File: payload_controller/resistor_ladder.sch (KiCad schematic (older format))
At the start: 35 parts, among them U1 74HC590, U10 ADG841YKSZ-500RL7, U10 OPA2387, U11 ADG841YKSZ-500RL7, U11 MCP4725xxx-xCH, U12 ADG841YKSZ-500RL7, U13 ADG841YKSZ-500RL7, U6 ADG841YKSZ-500RL7, U7 ADG841YKSZ-500RL7, U8 ADG841YKSZ-500RL7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

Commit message: Continuing layout
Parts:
- removed U10: OPA2387, Package_SON:WSON-8-1EP_2x2mm_P0.5mm_EP0.9x1.6mm, symbol OPA2387:OPA2387
- added unit 2 of U10
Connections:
- net -3V3: now also U10.9 (TP)
- net V_PANEL: now also U10.5 (+), U10.7
- net at R11.2, R13.1, R14.1: now also U10.6 (-)
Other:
- moved on the sheet: R13, R14
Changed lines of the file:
@@
 	-1   0    0    1
-$EndComp
-$Comp
-L Device:R R14
-U 1 1 6395E4CC
-P 9550 2700
-F 0 "R14" V 9650 2700 50  0000 C CNN
-F 1 "100k" V 9550 2700 50  0000 C CNN
-F 2 "Resistor_SMD:R_0603_1608Metric" V 9480 2700 50  0001 C CNN
-F 3 "~" H 9550 2700 50  0001 C CNN
-	1    9550 2700
-	0    -1   -1   0
-$EndComp
-$Comp
-L power:GND #PWR0134
-U 1 1 6395EDA9
-P 9700 2700
-F 0 "#PWR0134" H 9700 2450 50  0001 C CNN
-F 1 "GND" H 9705 2527 50  0000 C CNN
-F 2 "" H 9700 2700 50  0001 C CNN
-F 3 "" H 9700 2700 50  0001 C CNN
-	1    9700 2700
-	0    -1   -1   0
 $EndComp
 Wire Wire Line
@@
 Wire Wire Line
 	9500 1350 9500 1550
-$Comp
-L power:-3V3 #PWR?
-U 1 1 638EAACA
-P 9700 2500
-AR Path="/63C503EE/638EAACA" Ref="#PWR?"  Part="1"
-AR Path="/635FEB2F/638EAACA" Ref="#PWR0136"  Part="1"
-F 0 "#PWR0136" H 9700 2600 50  0001 C CNN
-F 1 "-3V3" V 9715 2628 50  0000 L CNN
-F 2 "" H 9700 2500 50  0001 C CNN
-F 3 "" H 9700 2500 50  0001 C CNN
-	1    9700 2500
-	0    1    1    0
-$EndComp
 Wire Wire Line
 	9650 2300 10000 2300
@@
 Wire Wire Line
 	10000 1550 9500 1550
-$Comp
-L Device:R R13
-U 1 1 6391F434
-P 9550 2500
-F 0 "R13" V 9650 2500 50  0000 C CNN
-F 1 "500k" V 9550 2500 50  0000 C CNN
-F 2 "Resistor_SMD:R_0603_1608Metric" V 9480 2500 50  0001 C CNN
-F 3 "~" H 9550 2500 50  0001 C CNN
-	1    9550 2500
-	0    -1   -1   0
-$EndComp
 Connection ~ 9500 1350
 Wire Wire Line
 	9500 1350 9950 1350
-Wire Wire Line
-	9350 2300 9350 2500
-Wire Wire Line
-	9400 2700 9350 2700
-Wire Wire Line
-	9400 2500 9350 2500
-Connection ~ 9350 2500
-Wire Wire Line
-	9350 2500 9350 2700
-Wire Wire Line
-	9350 2800 9350 2700
-Connection ~ 9350 2700
 Wire Wire Line
 	9450 3900 9450 4100
@@
 	9350 3900 9350 5650
 Wire Notes Line
-	8750 1450 8750 4850
+	8650 1450 8650 4850
 Wire Notes Line
 	8750 4850 10350 4850
@@
 	1700 3750 2050 3750
 $Comp
-L OPA2387:OPA2387 U10
-U 1 1 6382E466
-P 9500 2050
-F 0 "U10" V 9800 1950 50  0000 R CNN
-F 1 "OPA2387" V 9700 1950 50  0000 R CNN
-F 2 "Package_SON:WSON-8-1EP_2x2mm_P0.5mm_EP0.9x1.6mm" H 9900 2250 50  0001 C CNN
-F 3 "" H 9900 2250 50  0001 C CNN
-	1    9500 2050
-	0    -1   -1   0
-$EndComp
-Connection ~ 9500 1550
-$Comp
 L power:-3V3 #PWR?
 U 1 1 6383D96E
-P 9850 1950
+P 9500 2300
 AR Path="/63C503EE/6383D96E" Ref="#PWR?"  Part="1"
 AR Path="/635FEB2F/6383D96E" Ref="#PWR0128"  Part="1"
-F 0 "#PWR0128" H 9850 2050 50  0001 C CNN
-F 1 "-3V3" V 9865 2078 50  0000 L CNN
-F 2 "" H 9850 1950 50  0001 C CNN
-F 3 "" H 9850 1950 50  0001 C CNN
-	1    9850 1950
+F 0 "#PWR0128" H 9500 2400 50  0001 C CNN
+F 1 "-3V3" V 9515 2428 50  0000 L CNN
+F 2 "" H 9500 2300 50  0001 C CNN
+F 3 "" H 9500 2300 50  0001 C CNN
+	1    9500 2300
 	-1   0    0    1
 $EndComp
-$Comp
-L power:+3V3 #PWR0135
-U 1 1 6383DF99
-P 9150 1950
-F 0 "#PWR0135" H 9150 1800 50  0001 C CNN
-F 1 "+3V3" H 9165 2123 50  0000 C CNN
-F 2 "" H 9150 1950 50  0001 C CNN
-F 3 "" H 9150 1950 50  0001 C CNN
-	1    9150 1950
-	1    0    0    -1
-$EndComp
-Wire Wire Line
-	9850 1950 9800 1950
-Wire Wire Line
-	9150 1950 9200 1950
 Connection ~ 3950 1750
 Wire Wire Line
@@
 	0    1    1    0
 $EndComp
+$Comp
+L OPA2387:OPA2387 U?
+U 2 1 63A95D48
+P 9500 2050
+AR Path="/63C503EE/63A95D48" Ref="U?"  Part="2"
+AR Path="/635FEB2F/63A95D48" Ref="U10"  Part="2"
+F 0 "U10" H 9750 2350 50  0000 C CNN
+F 1 "OPA2387" H 9800 2250 50  0000 C CNN
+F 2 "Package_SON:WSON-8-1EP_2x2mm_P0.5mm_EP0.9x1.6mm" H 9900 2250 50  0001 C CNN
+F 3 "" H 9900 2250 50  0001 C CNN
+	2    9500 2050
+	0    1    -1   0
+$EndComp
+Connection ~ 9500 1550
+Connection ~ 9350 2700
+Connection ~ 9350 2500
+Wire Wire Line
+	9350 2300 9350 2500
+Wire Wire Line
+	9350 2800 9350 2700
+Wire Wire Line
+	9350 2500 9350 2700
+Wire Wire Line
+	9300 2700 9350 2700
+Wire Wire Line
+	9300 2500 9350 2500
+$Comp
+L Device:R R13
+U 1 1 6391F434
+P 9150 2700
+F 0 "R13" V 9250 2700 50  0000 C CNN
+F 1 "500k" V 9150 2700 50  0000 C CNN
+F 2 "Resistor_SMD:R_0603_1608Metric" V 9080 2700 50  0001 C CNN
+F 3 "~" H 9150 2700 50  0001 C CNN
+	1    9150 2700
+	0    1    1    0
+$EndComp
+$Comp
+L power:-3V3 #PWR?
+U 1 1 638EAACA
+P 9000 2700
+AR Path="/63C503EE/638EAACA" Ref="#PWR?"  Part="1"
+AR Path="/635FEB2F/638EAACA" Ref="#PWR0136"  Part="1"
+F 0 "#PWR0136" H 9000 2800 50  0001 C CNN
+F 1 "-3V3" V 9015 2828 50  0000 L CNN
+F 2 "" H 9000 2700 50  0001 C CNN
+F 3 "" H 9000 2700 50  0001 C CNN
+	1    9000 2700
+	0    -1   -1   0
+$EndComp
+$Comp
+L power:GND #PWR0134
+U 1 1 6395EDA9
+P 9000 2500
+F 0 "#PWR0134" H 9000 2250 50  0001 C CNN
+F 1 "GND" H 9005 2327 50  0000 C CNN
+F 2 "" H 9000 2500 50  0001 C CNN
+F 3 "" H 9000 2500 50  0001 C CNN
+	1    9000 2500
+	0    1    1    0
+$EndComp
+$Comp
+L Device:R R14
+U 1 1 6395E4CC
+P 9150 2500
+F 0 "R14" V 9250 2500 50  0000 C CNN
+F 1 "100k" V 9150 2500 50  0000 C CNN
+F 2 "Resistor_SMD:R_0603_1608Metric" V 9080 2500 50  0001 C CNN
+F 3 "~" H 9150 2500 50  0001 C CNN
+	1    9150 2500
+	0    1    1    0
+$EndComp

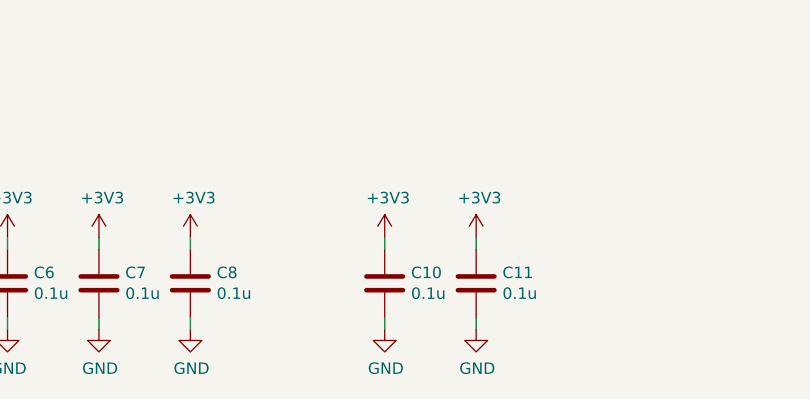
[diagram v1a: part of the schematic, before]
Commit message: Continuing payload design
- Add OR gate for reverse bias
- Add GaAs panel connectors
- Add 3D models
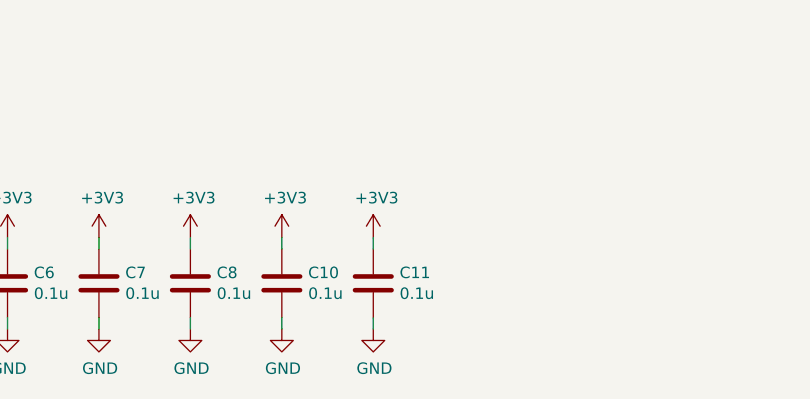
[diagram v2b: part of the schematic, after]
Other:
- moved on the sheet: C10, C11
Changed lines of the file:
@@
 	3350 1750 3350 2050
 Wire Wire Line
-	5400 7100 5400 7150
+	4950 7100 4950 7150
 Wire Wire Line
-	5400 6750 5400 6800
+	4950 6750 4950 6800
 $Comp
 L power:GND #PWR0124
 U 1 1 63873538
-P 5400 7150
-F 0 "#PWR0124" H 5400 6900 50  0001 C CNN
-F 1 "GND" H 5405 6977 50  0000 C CNN
-F 2 "" H 5400 7150 50  0001 C CNN
-F 3 "" H 5400 7150 50  0001 C CNN
-	1    5400 7150
+P 4950 7150
+F 0 "#PWR0124" H 4950 6900 50  0001 C CNN
+F 1 "GND" H 4955 6977 50  0000 C CNN
+F 2 "" H 4950 7150 50  0001 C CNN
+F 3 "" H 4950 7150 50  0001 C CNN
+	1    4950 7150
 	1    0    0    -1
 $EndComp
@@
 L power:+3V3 #PWR0125
 U 1 1 6387353E
-P 5400 6750
-F 0 "#PWR0125" H 5400 6600 50  0001 C CNN
-F 1 "+3V3" H 5415 6923 50  0000 C CNN
-F 2 "" H 5400 6750 50  0001 C CNN
-F 3 "" H 5400 6750 50  0001 C CNN
-	1    5400 6750
+P 4950 6750
+F 0 "#PWR0125" H 4950 6600 50  0001 C CNN
+F 1 "+3V3" H 4965 6923 50  0000 C CNN
+F 2 "" H 4950 6750 50  0001 C CNN
+F 3 "" H 4950 6750 50  0001 C CNN
+	1    4950 6750
 	1    0    0    -1
 $EndComp
@@
 L Device:C C10
 U 1 1 63873544
-P 5400 6950
-F 0 "C10" H 5515 6996 50  0000 L CNN
-F 1 "0.1u" H 5515 6905 50  0000 L CNN
-F 2 "Capacitor_SMD:C_0603_1608Metric" H 5438 6800 50  0001 C CNN
-F 3 "~" H 5400 6950 50  0001 C CNN
-	1    5400 6950
+P 4950 6950
+F 0 "C10" H 5065 6996 50  0000 L CNN
+F 1 "0.1u" H 5065 6905 50  0000 L CNN
+F 2 "Capacitor_SMD:C_0603_1608Metric" H 4988 6800 50  0001 C CNN
+F 3 "~" H 4950 6950 50  0001 C CNN
+	1    4950 6950
 	1    0    0    -1
 $EndComp
@@
 	1700 5650 2150 5650
 Wire Wire Line
-	5800 7100 5800 7150
+	5350 7100 5350 7150
 Wire Wire Line
-	5800 6750 5800 6800
+	5350 6750 5350 6800
 $Comp
 L power:GND #PWR0129
 U 1 1 6392E1EA
-P 5800 7150
-F 0 "#PWR0129" H 5800 6900 50  0001 C CNN
-F 1 "GND" H 5805 6977 50  0000 C CNN
-F 2 "" H 5800 7150 50  0001 C CNN
-F 3 "" H 5800 7150 50  0001 C CNN
-	1    5800 7150
+P 5350 7150
+F 0 "#PWR0129" H 5350 6900 50  0001 C CNN
+F 1 "GND" H 5355 6977 50  0000 C CNN
+F 2 "" H 5350 7150 50  0001 C CNN
+F 3 "" H 5350 7150 50  0001 C CNN
+	1    5350 7150
 	1    0    0    -1
 $EndComp
@@
 L power:+3V3 #PWR0130
 U 1 1 6392E1F0
-P 5800 6750
-F 0 "#PWR0130" H 5800 6600 50  0001 C CNN
-F 1 "+3V3" H 5815 6923 50  0000 C CNN
-F 2 "" H 5800 6750 50  0001 C CNN
-F 3 "" H 5800 6750 50  0001 C CNN
-	1    5800 6750
+P 5350 6750
+F 0 "#PWR0130" H 5350 6600 50  0001 C CNN
+F 1 "+3V3" H 5365 6923 50  0000 C CNN
+F 2 "" H 5350 6750 50  0001 C CNN
+F 3 "" H 5350 6750 50  0001 C CNN
+	1    5350 6750
 	1    0    0    -1
 $EndComp
@@
 L Device:C C11
 U 1 1 6392E1F6
-P 5800 6950
-F 0 "C11" H 5915 6996 50  0000 L CNN
-F 1 "0.1u" H 5915 6905 50  0000 L CNN
-F 2 "Capacitor_SMD:C_0603_1608Metric" H 5838 6800 50  0001 C CNN
-F 3 "~" H 5800 6950 50  0001 C CNN
-	1    5800 6950
+P 5350 6950
+F 0 "C11" H 5465 6996 50  0000 L CNN
+F 1 "0.1u" H 5465 6905 50  0000 L CNN
+F 2 "Capacitor_SMD:C_0603_1608Metric" H 5388 6800 50  0001 C CNN
+F 3 "~" H 5350 6950 50  0001 C CNN
+	1    5350 6950
 	1    0    0    -1
 $EndComp

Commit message: Generated manufacturing files
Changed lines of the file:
@@
 Sheet 2 6
 Title "Resistor 8-Bit Ladder"
-Date "2022-09-18"
+Date "2022-11-30"
 Rev "B"
 Comp "Advanced eXperimental Payloads | UNL Aerospace Club"
 Comment1 "Copyright (c) 2022"
 Comment2 "Designer: WSA"
-Comment3 "Reviewer:"
-Comment4 "Approved: "
+Comment3 "Reviewer: WSA"
+Comment4 "Approved: WSA"
 $EndDescr
 $Comp
@@
 	8650 1450 8650 4850
 Wire Notes Line
-	8750 4850 10350 4850
-Wire Notes Line
 	10350 4850 10350 1450
-Wire Notes Line
-	8750 1450 10350 1450
 Text Notes 10250 4750 2    50   ~ 0
 1.2V to -0.3V\nPanel Voltage Drive
@@
 	0    1    1    0
 $EndComp
+Wire Notes Line
+	8650 4850 10350 4850
+Wire Notes Line
+	8650 1450 10350 1450
 $EndSCHEMATC
